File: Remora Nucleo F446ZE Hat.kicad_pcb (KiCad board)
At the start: 2 copper layers, 108.2 x 137.1 mm, 95 parts, among them J1 NucleoF446ZE CN11 Header, J10 A_STEP_AND_DIR+-, J11 B_STEP_AND_DIR+-, J12 C_STEP_AND_DIR+-, J13 DIGITAL_OUTPUTS, J15 Digital Inputs, J16 5V External Power Inlet, J17 9V External Power Inlet, J2 MSD-1-A, J3 UART_TX, J4 NucleoF446ZE CN12 Header, J7 X_STEP_AND_DIR+-, J8 Y_STEP_AND_DIR+-, J9 Z_STEP_AND_DIR+-, SW1 SW_Push, U10 ADUM1201ARZ, U11 HT26LS31ARZ, U12 ADUM1201ARZ, U13 ADUM1201ARZ, U14 HT26LS31ARZ, U19 LTV-247, U20 LTV-247, U21 LTV-247, U22 LTV-247, U4 ADUM1201ARZ, U5 ADUM1201ARZ, U6 HT26LS31ARZ, U7 LTV-247, U8 LTV-247, U9 ADUM1201ARZ

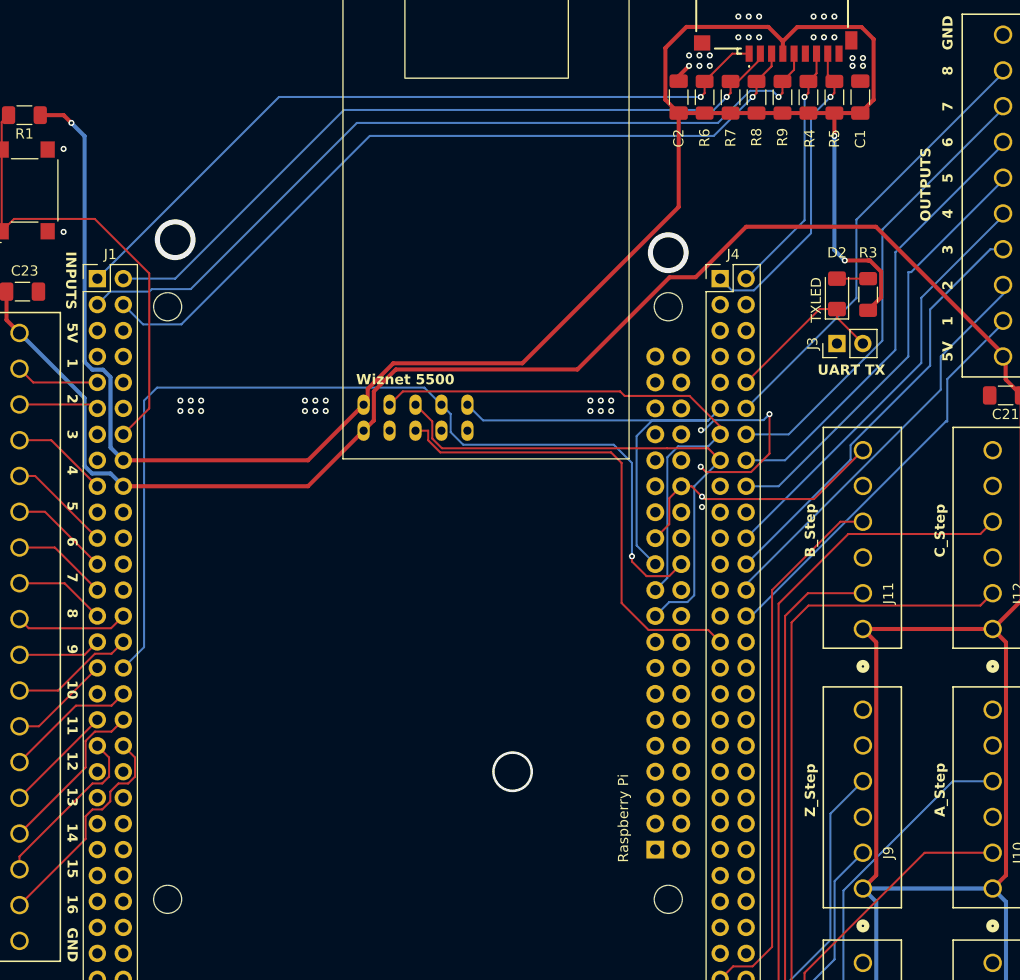
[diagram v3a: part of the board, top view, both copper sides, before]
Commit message: Renumbered IO to start at 0 to match firmware
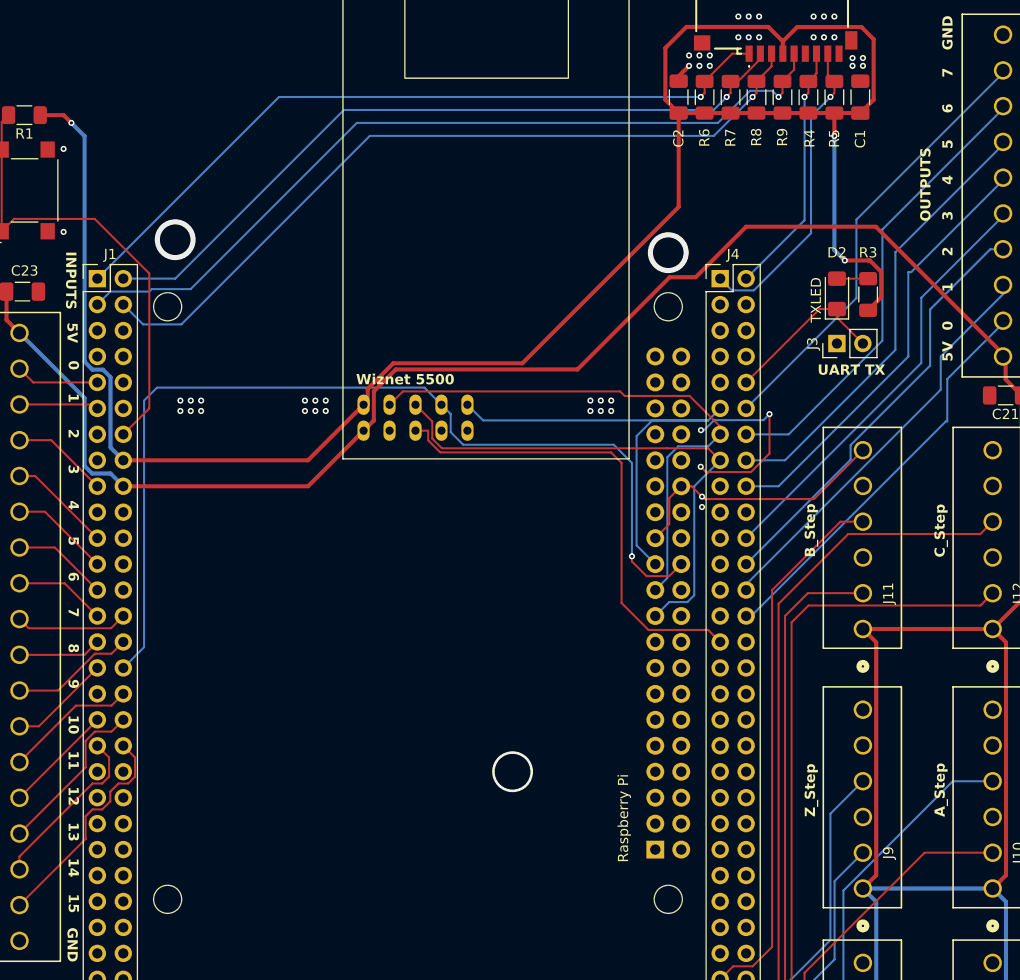
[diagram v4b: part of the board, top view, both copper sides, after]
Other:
- board text added: "0"
- board text removed: "16"
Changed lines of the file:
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@@
 	)
 	(gr_text "1"
-		(at 103.632 73.827 270)
+		(at 103.749339 77.238 270)
 		(layer "F.SilkS")
 		(effects
@@
 	)
 	(gr_text "14"
-		(at 103.632 119.327 270)
+		(at 103.749339 122.738 270)
 		(layer "F.SilkS")
 		(effects
@@
 	)
 	(gr_text "13"
-		(at 103.632 115.827 270)
+		(at 103.749339 119.238 270)
 		(layer "F.SilkS")
 		(effects
@@
 	)
 	(gr_text "1"
-		(at 190.5 70.668 90)
+		(at 190.5 67.355 90)
 		(layer "F.SilkS")
 		(effects
@@
 	)
 	(gr_text "10"
-		(at 103.632 105.327 270)
+		(at 103.749339 108.738 270)
 		(layer "F.SilkS")
 		(effects
@@
 	)
 	(gr_text "7"
-		(at 190.5 49.668 90)
+		(at 190.5 46.355 90)
 		(layer "F.SilkS")
 		(effects
@@
 	)
 	(gr_text "5"
-		(at 103.632 87.827 270)
+		(at 103.749339 91.238 270)
 		(layer "F.SilkS")
 		(effects
@@
 	)
 	(gr_text "15"
-		(at 103.641661 122.827 270)
+		(at 103.759 126.238 270)
 		(layer "F.SilkS")
 		(effects
@@
 	)
 	(gr_text "4"
-		(at 103.632 84.327 270)
+		(at 103.749339 87.738 270)
 		(layer "F.SilkS")
 		(effects
@@
 	)
 	(gr_text "5"
-		(at 190.5 56.668 90)
+		(at 190.5 53.355 90)
 		(layer "F.SilkS")
 		(effects
@@
 	)
 	(gr_text "7"
-		(at 103.632 94.827 270)
+		(at 103.749339 98.238 270)
 		(layer "F.SilkS")
 		(effects
@@
 		)
 	)
-	(gr_text "8"
-		(at 190.5 46.168 90)
+	(gr_text "0"
+		(at 103.759 74.041 270)
 		(layer "F.SilkS")
 		(effects
@@
 	)
 	(gr_text "2"
-		(at 103.632 77.327 270)
+		(at 103.749339 80.738 270)
 		(layer "F.SilkS")
 		(effects
@@
 	)
 	(gr_text "6"
-		(at 103.632 91.327 270)
+		(at 103.749339 94.738 270)
 		(layer "F.SilkS")
 		(effects
@@
 	)
 	(gr_text "8"
-		(at 103.632 98.327 270)
+		(at 103.749339 101.738 270)
 		(layer "F.SilkS")
 		(effects
@@
 	)
 	(gr_text "9"
-		(at 103.632 101.827 270)
+		(at 103.749339 105.238 270)
 		(layer "F.SilkS")
 		(effects
@@
 	)
 	(gr_text "2"
-		(at 190.5 67.168 90)
+		(at 190.5 63.855 90)
 		(layer "F.SilkS")
 		(effects
@@
 	)
 	(gr_text "4"
-		(at 190.5 60.168 90)
+		(at 190.5 56.855 90)
 		(layer "F.SilkS")
 		(effects
@@
 	)
 	(gr_text "3"
-		(at 190.5 63.668 90)
+		(at 190.5 60.355 90)
 		(layer "F.SilkS")
 		(effects
@@
 	)
 	(gr_text "3"
-		(at 103.632 80.827 270)
+		(at 103.749339 84.238 270)
 		(layer "F.SilkS")
 		(effects
@@
 	)
 	(gr_text "11"
-		(at 103.632 108.827 270)
+		(at 103.749339 112.238 270)
 		(layer "F.SilkS")
 		(effects
@@
 	)
 	(gr_text "12"
-		(at 103.632 112.327 270)
+		(at 103.749339 115.738 270)
 		(layer "F.SilkS")
 		(effects
@@
 	)
 	(gr_text "6"
-		(at 190.5 53.168 90)
+		(at 190.5 49.855 90)
 		(layer "F.SilkS")
 		(effects
@@
 		)
 	)
-	(gr_text "16"
-		(at 103.641661 126.327 270)
-		(layer "F.SilkS")
-		(effects
+	(gr_text "0"
+		(at 190.5 71.12 90)
+		(layer "F.SilkS")
+		(effects

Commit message: more BOM consolidation. Switched out IO for vertical toolless wire to board terminals and added footprints. Put new isolated ground plane on board.
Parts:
- J16: value 5V External Power Inlet -> 5V EXT
- J17: value 9V External Power Inlet -> 9V EXT
- moved F1 198.9 mm to (257.3, 33.3)
- moved F2 198.9 mm to (257.3, 35.8)
- moved F3 198.9 mm to (257.3, 38.3)
- moved F4 198.9 mm to (257.3, 40.8)
- moved C13 198.9 mm to (241.9, 48.9)
- moved C14 198.9 mm to (241.9, 52.3)
- moved C15 198.9 mm to (241.9, 55.6)
- moved C16 198.9 mm to (241.9, 59.0)
- moved F5 198.9 mm to (235.5, 33.3)
- moved F6 198.9 mm to (235.5, 35.8)
- moved F7 198.9 mm to (235.5, 38.3)
- moved F8 198.9 mm to (235.5, 40.8)
- moved R16 198.9 mm to (242.6, 33.7)
- moved R17 198.9 mm to (242.6, 37.0)
- moved R18 198.9 mm to (242.6, 40.3)
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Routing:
- net +5VD: track 299.9 -> 0.00 mm
- net +3V3: track 193.5 -> 0.00 mm, vias 3 -> 1
- net /SPI1_CS: track 94.9 -> 0.00 mm, vias 1 -> 0
- net /SDIO_CLK: track 80.5 -> 0.00 mm, vias 1 -> 0
- net /SDIO_CMD: track 76.6 -> 0.00 mm, vias 1 -> 0
- net /SDIO_D2: track 73.6 -> 0.00 mm, vias 1 -> 0
- net /SDIO_D3: track 72.5 -> 0.00 mm, vias 1 -> 0
- net /MCU_C_DIR: track 67.4 -> 0.00 mm
- net /MCU_C_STEP: track 65.8 -> 0.00 mm
- net /MCU_B_STEP: track 57.2 -> 0.00 mm
- net /SPI1_MISO: track 54.7 -> 0.00 mm
- net /MCU_B_DIR: track 53.0 -> 0.00 mm
- net /SPI1_MOSI: track 52.0 -> 0.00 mm
- net /WIZ_RST: track 47.4 -> 0.00 mm
- net GNDREF: track 47.2 -> 0.00 mm, vias 56 -> 9
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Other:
- board size 108.2 x 137.1 mm -> 108 x 162 mm
- board text added: "STATUS"
- board text removed: "USR LED"

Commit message: Swapped out stepper isolators to use same as others. further BOM consolidation. Fixed bug with incorrect differential driver footprint.
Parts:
- removed C10, C16, C17, C18, C20, C9: 100nF, Capacitor_SMD:C_1206_3216Metric_Pad1.33x1.80mm_HandSolder
- removed R1: 10K, Resistor_SMD:R_1206_3216Metric_Pad1.30x1.75mm_HandSolder
- removed R15: 150R, Resistor_SMD:R_1206_3216Metric_Pad1.30x1.75mm_HandSolder
- removed R16, R17, R18, R19, R20, R21, R22, R23: 120R, Resistor_SMD:R_1206_3216Metric_Pad1.30x1.75mm_HandSolder
- removed R2, R3: 100R, Resistor_SMD:R_1206_3216Metric_Pad1.30x1.75mm_HandSolder
- removed U10, U12, U13: ADUM1201ARZ, Package_SO:SOIC-8_3.9x4.9mm_P1.27mm
- added J18: Conn_01x04_Socket, Amphenol QT:QT04ADP83V0000G, F.Cu at (352.0, 76.3)
- added J19: Conn_01x02_Socket, Amphenol QT:QT02ADP83V0000G, F.Cu at (336.9, 9.77)
- added J20: Conn_01x04_Socket, Amphenol QT:QT04ADP83V0000G, F.Cu at (313.8, 9.77)
- added J21: Conn_01x04_Socket, Amphenol QT:QT04ADP83V0000G, F.Cu at (313.8, 25.9)
- added J22: Conn_01x04_Socket, Amphenol QT:QT04ADP83V0000G, F.Cu at (313.8, 42.0)
- added J23: Conn_01x04_Socket, Amphenol QT:QT04ADP83V0000G, F.Cu at (313.8, 58.1)
- added J24: Conn_01x04_Socket, Amphenol QT:QT04ADP83V0000G, F.Cu at (313.8, 76.3)
- added J25: Conn_01x02_Socket, Amphenol QT:QT02ADP83V0000G, F.Cu at (336.9, 76.3)
- added J26: Conn_01x04_Socket, Amphenol QT:QT04ADP83V0000G, F.Cu at (313.8, 92.4)
- added J27: Conn_01x02_Socket, Amphenol QT:QT02ADP83V0000G, F.Cu at (365.1, 92.4)
- added J28: Conn_01x04_Socket, Amphenol QT:QT04ADP83V0000G, F.Cu at (386.7, 25.9)
- added J29: Conn_01x02_Socket, Amphenol QT:QT02ADP83V0000G, F.Cu at (399.8, 42.0)
- added R44: 4K7, Resistor_SMD:R_1206_3216Metric_Pad1.30x1.75mm_HandSolder, F.Cu at (392.5, 89.4)
- added R45: 180R, Resistor_SMD:R_1206_3216Metric_Pad1.30x1.75mm_HandSolder, F.Cu at (392.5, 74.2)
- added R46: 180R, Resistor_SMD:R_1206_3216Metric_Pad1.30x1.75mm_HandSolder, F.Cu at (384.5, 74.2)
- added R47: 180R, Resistor_SMD:R_1206_3216Metric_Pad1.30x1.75mm_HandSolder, F.Cu at (392.5, 77.5)
- added R48: 180R, Resistor_SMD:R_1206_3216Metric_Pad1.30x1.75mm_HandSolder, F.Cu at (384.5, 77.5)
- added R49: 180R, Resistor_SMD:R_1206_3216Metric_Pad1.30x1.75mm_HandSolder, F.Cu at (392.5, 80.8)
- added R50: 180R, Resistor_SMD:R_1206_3216Metric_Pad1.30x1.75mm_HandSolder, F.Cu at (384.5, 80.8)
- added R51: 180R, Resistor_SMD:R_1206_3216Metric_Pad1.30x1.75mm_HandSolder, F.Cu at (392.5, 84.1)
- added R52: 180R, Resistor_SMD:R_1206_3216Metric_Pad1.30x1.75mm_HandSolder, F.Cu at (384.5, 84.1)
- added R53: 180R, Resistor_SMD:R_1206_3216Metric_Pad1.30x1.75mm_HandSolder, F.Cu at (392.5, 92.8)
- added R54: 180R, Resistor_SMD:R_1206_3216Metric_Pad1.30x1.75mm_HandSolder, F.Cu at (392.5, 96.1)
- added R55: 180R, Resistor_SMD:R_1206_3216Metric_Pad1.30x1.75mm_HandSolder, F.Cu at (384.5, 68.9)
- added R56: 180R, Resistor_SMD:R_1206_3216Metric_Pad1.30x1.75mm_HandSolder, F.Cu at (376.1, 34.7)
- added R57: 180R, Resistor_SMD:R_1206_3216Metric_Pad1.30x1.75mm_HandSolder, F.Cu at (376.1, 85.0)
- added R58: 180R, Resistor_SMD:R_1206_3216Metric_Pad1.30x1.75mm_HandSolder, F.Cu at (410.8, 34.7)
- added R59: 180R, Resistor_SMD:R_1206_3216Metric_Pad1.30x1.75mm_HandSolder, F.Cu at (376.1, 38.0)
- added R60: 180R, Resistor_SMD:R_1206_3216Metric_Pad1.30x1.75mm_HandSolder, F.Cu at (376.1, 88.3)
- added R61: 180R, Resistor_SMD:R_1206_3216Metric_Pad1.30x1.75mm_HandSolder, F.Cu at (410.8, 38.0)
- added R62: 180R, Resistor_SMD:R_1206_3216Metric_Pad1.30x1.75mm_HandSolder, F.Cu at (376.1, 41.3)
- added R63: 180R, Resistor_SMD:R_1206_3216Metric_Pad1.30x1.75mm_HandSolder, F.Cu at (376.1, 91.6)
- added R64: 180R, Resistor_SMD:R_1206_3216Metric_Pad1.30x1.75mm_HandSolder, F.Cu at (410.8, 41.3)
- added R65: 180R, Resistor_SMD:R_1206_3216Metric_Pad1.30x1.75mm_HandSolder, F.Cu at (376.1, 44.6)
- added R66: 180R, Resistor_SMD:R_1206_3216Metric_Pad1.30x1.75mm_HandSolder, F.Cu at (376.1, 94.9)
- added R67: 180R, Resistor_SMD:R_1206_3216Metric_Pad1.30x1.75mm_HandSolder, F.Cu at (410.8, 44.6)
- D1: value USR_LED -> LED
- D2: value TXLED -> LED
- D5: value 9VLED -> LED
- D6: value 5VLED -> LED
- J1: value NucleoF446ZE CN11 Header -> Conn_02x35_Odd_Even
- J10: value A_STEP_AND_DIR+- -> Conn_01x02_Socket; footprint EBWA_06_A:CONN_EBWA-06-A_ADM -> Amphenol QT:QT02ADP83V0000G
- J11: value B_STEP_AND_DIR+- -> Conn_01x04_Socket; footprint EBWA_06_A:CONN_EBWA-06-A_ADM -> Amphenol QT:QT04ADP83V0000G
- J12: value C_STEP_AND_DIR+- -> Conn_01x02_Socket; footprint EBWA_06_A:CONN_EBWA-06-A_ADM -> Amphenol QT:QT02ADP83V0000G
- J13: value DIGITAL_OUTPUTS -> Conn_01x02_Socket; footprint EBWA_06_A:CONN_EBWA-10-A_ADM -> Amphenol QT:QT02ADP83V0000G
- J15: value Digital Inputs -> Conn_01x02_Socket; footprint EBWA_06_A:CONN_EBWA-18-A_ADM -> Amphenol QT:QT02ADP83V0000G
- J16: value 5V EXT -> Conn_01x04_Socket; footprint EBWA_02_A:ADAMTECH_EBWA-02-A -> Amphenol QT:QT04ADP83V0000G
- J17: value 9V EXT -> Conn_01x02_Socket; footprint EBWA_02_A:ADAMTECH_EBWA-02-A -> Amphenol QT:QT02ADP83V0000G
- J4: value NucleoF446ZE CN12 Header -> Conn_02x35_Odd_Even
- J7: value X_STEP_AND_DIR+- -> Conn_01x04_Socket; footprint EBWA_06_A:CONN_EBWA-06-A_ADM -> Amphenol QT:QT04ADP83V0000G
- J8: value Y_STEP_AND_DIR+- -> Conn_01x02_Socket; footprint EBWA_06_A:CONN_EBWA-06-A_ADM -> Amphenol QT:QT02ADP83V0000G
- J9: value Z_STEP_AND_DIR+- -> Conn_01x04_Socket; footprint EBWA_06_A:CONN_EBWA-06-A_ADM -> Amphenol QT:QT04ADP83V0000G
- RP1: value Raspberry_Pi_2_3 -> Raspberry_Pi_Header
- U1: value ~ -> Wiznet W5500 Eval Module
- U11, U14, U6: value HT26LS31ARZ -> AM26LS31CDR; footprint Package_DIP:SMDIP-4_W9.53mm -> Package_SO:SOIC-16_3.9x9.9mm_P1.27mm
- U4, U5, U9: value ADUM1201ARZ -> LTV-247; footprint Package_SO:SOIC-8_3.9x4.9mm_P1.27mm -> Package_SO:SOP-16_4.4x10.4mm_P1.27mm
- moved J15 236.1 mm to (399.8, 60.1), turned to 0 degrees
- moved J17 235.1 mm to (365.1, 42.0)
- moved J16 234.4 mm to (352.0, 25.9)
- moved J13 222.1 mm to (386.7, 60.1), turned to 0 degrees
- moved J11 219.0 mm to (386.7, 9.77), turned to 0 degrees
- moved J7 217.2 mm to (352.0, 9.77), turned to 0 degrees
- moved U9 207.5 mm to (409.4, 6.74)
- moved J12 195.4 mm to (386.7, 42.0), turned to 0 degrees
- moved J8 187.1 mm to (352.0, 42.0), turned to 0 degrees
- moved J9 177.3 mm to (352.0, 60.1), turned to 0 degrees
- moved C14 170.1 mm to (407.7, 14.4)
- moved U4 160.0 mm to (374.8, 6.74)
- moved C12 158.6 mm to (373.0, 14.4)
- moved J10 155.3 mm to (352.0, 92.4), turned to 0 degrees
- moved U5 134.9 mm to (374.8, 57.1)
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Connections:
- C13 pad 1: GNDREF -> +5VD
- C13 pad 2: +3V3 -> GNDPWR
- C14 pad 1: GNDREF -> +5VD
- C14 pad 2: +3V3 -> GNDPWR
- F1 pad 2: /Digital Outputs/4CH digital output driver 1/OUTPUT1 -> /Digital Outputs/4CH digital output driver 1/OUTPUT0
- F2 pad 2: /Digital Outputs/4CH digital output driver 1/OUTPUT2 -> /Digital Outputs/4CH digital output driver 1/OUTPUT1
- F3 pad 2: /Digital Outputs/4CH digital output driver 1/OUTPUT3 -> /Digital Outputs/4CH digital output driver 1/OUTPUT2
- F4 pad 2: /Digital Outputs/4CH digital output driver 1/OUTPUT4 -> /Digital Outputs/4CH digital output driver 1/OUTPUT3
- F5 pad 2: /Digital Outputs/4CH digital output driver 2/OUTPUT5 -> /Digital Outputs/4CH digital output driver 2/OUTPUT4
- F6 pad 2: /Digital Outputs/4CH digital output driver 2/OUTPUT6 -> /Digital Outputs/4CH digital output driver 2/OUTPUT5
- F7 pad 2: /Digital Outputs/4CH digital output driver 2/OUTPUT7 -> /Digital Outputs/4CH digital output driver 2/OUTPUT6
- F8 pad 2: /Digital Outputs/4CH digital output driver 2/OUTPUT8 -> /Digital Outputs/4CH digital output driver 2/OUTPUT7
- J1 pad 11: MCU_DIGITAL_IN_2 -> MCU_DIGITAL_IN_1
- J1 pad 17: MCU_DIGITAL_IN_3 -> MCU_DIGITAL_IN_2
- J1 pad 21: MCU_DIGITAL_IN_4 -> MCU_DIGITAL_IN_3
- J1 pad 23: MCU_DIGITAL_IN_5 -> MCU_DIGITAL_IN_4
- J1 pad 25: MCU_DIGITAL_IN_6 -> unconnected-(J1-Pin_25-Pad25)
- J1 pad 27: MCU_DIGITAL_IN_7 -> unconnected-(J1-Pin_27-Pad27)
- J1 pad 28: MCU_DIGITAL_IN_8 -> MCU_DIGITAL_IN_5
- J1 pad 29: MCU_DIGITAL_IN_9 -> unconnected-(J1-Pin_29-Pad29)
- J1 pad 30: MCU_DIGITAL_IN_10 -> MCU_DIGITAL_IN_6
- J1 pad 31: MCU_DIGITAL_IN_11 -> unconnected-(J1-Pin_31-Pad31)
- J1 pad 34: MCU_DIGITAL_IN_12 -> MCU_DIGITAL_IN_7
- J1 pad 35: MCU_DIGITAL_IN_13 -> MCU_DIGITAL_IN_8
- J1 pad 36: MCU_DIGITAL_IN_14 -> MCU_DIGITAL_IN_9
- J1 pad 37: MCU_DIGITAL_IN_15 -> MCU_DIGITAL_IN_10
- J1 pad 38: MCU_DIGITAL_IN_16 -> MCU_DIGITAL_IN_11
- J1 pad 39: unconnected-(J1-Pin_39-Pad39) -> MCU_DIGITAL_IN_12
- J1 pad 40: unconnected-(J1-Pin_40-Pad40) -> MCU_DIGITAL_IN_13
- J1 pad 41: unconnected-(J1-Pin_41-Pad41) -> MCU_DIGITAL_IN_14
- J1 pad 42: unconnected-(J1-Pin_42-Pad42) -> MCU_DIGITAL_IN_15
- J1 pad 9: MCU_DIGITAL_IN_1 -> MCU_DIGITAL_IN_0
- J10 pad 1: +5VD -> /Z and A Stepper Drivers/A_DIR-
- J10 pad 2: /Z and A Stepper Drivers/A_STEP+ -> GNDPWR
- J11 pad 2: /B and C Stepper Drivers/B_STEP+ -> /B and C Stepper Drivers/C_STEP+
- J11 pad 3: /B and C Stepper Drivers/B_STEP- -> /B and C Stepper Drivers/C_STEP-
- J11 pad 4: /B and C Stepper Drivers/B_DIR+ -> /B and C Stepper Drivers/C_DIR+
- J12 pad 1: +5VD -> /B and C Stepper Drivers/C_DIR-
- J12 pad 2: /B and C Stepper Drivers/C_STEP+ -> GNDPWR
- J13 pad 1: +5VD -> GNDPWR
- J13 pad 2: /Digital Outputs/4CH digital output driver 1/OUTPUT1 -> +5VD
- J15 pad 1: +5VD -> GNDREF
- J15 pad 2: /Digital Inputs/Digital Input 1-4/INPUT1 -> +9V
- J16 pad 1: GNDPWR -> +5VD
- J16 pad 2: +5VD -> /X and Y Stepper Drivers/X_STEP+
- J17 pad 1: GNDREF -> /X and Y Stepper Drivers/X_DIR-
- J17 pad 2: +9V -> GNDPWR
- J4 pad 12: MCU_DIGITAL_OUT_8 -> unconnected-(J4-Pin_12-Pad12)
- J4 pad 16: MCU_DIGITAL_OUT_6 -> unconnected-(J4-Pin_16-Pad16)
- J4 pad 17: unconnected-(J4-Pin_17-Pad17) -> MCU_DIGITAL_OUT_6
- J4 pad 18: MCU_DIGITAL_OUT_5 -> unconnected-(J4-Pin_18-Pad18)
- J4 pad 21: unconnected-(J4-Pin_21-Pad21) -> MCU_DIGITAL_OUT_5
- J4 pad 22: MCU_DIGITAL_OUT_4 -> unconnected-(J4-Pin_22-Pad22)
- J4 pad 23: unconnected-(J4-Pin_23-Pad23) -> MCU_DIGITAL_OUT_4
- J4 pad 30: unconnected-(J4-Pin_30-Pad30) -> MCU_DIGITAL_OUT_0
- J4 pad 55: /MCU_B_DIR -> unconnected-(J4-Pin_55-Pad55)
- J4 pad 56: unconnected-(J4-Pin_56-Pad56) -> /MCU_C_DIR
- J4 pad 57: /MCU_B_STEP -> unconnected-(J4-Pin_57-Pad57)
- J4 pad 58: unconnected-(J4-Pin_58-Pad58) -> /MCU_C_STEP
- J4 pad 60: /MCU_C_DIR -> /MCU_B_DIR
- J4 pad 62: /MCU_C_STEP -> /MCU_B_STEP
- J4 pad 65: /USR_LED -> /STATUS_LED
- J7 pad 2: /X and Y Stepper Drivers/X_STEP+ -> /X and Y Stepper Drivers/Y_STEP+
- J7 pad 3: /X and Y Stepper Drivers/X_STEP- -> /X and Y Stepper Drivers/Y_STEP-
- J7 pad 4: /X and Y Stepper Drivers/X_DIR+ -> /X and Y Stepper Drivers/Y_DIR+
- J8 pad 1: +5VD -> /X and Y Stepper Drivers/Y_DIR-
- J8 pad 2: /X and Y Stepper Drivers/Y_STEP+ -> GNDPWR
- J9 pad 2: /Z and A Stepper Drivers/Z_STEP+ -> /Z and A Stepper Drivers/A_STEP+
- J9 pad 3: /Z and A Stepper Drivers/Z_STEP- -> /Z and A Stepper Drivers/A_STEP-
- J9 pad 4: /Z and A Stepper Drivers/Z_DIR+ -> /Z and A Stepper Drivers/A_DIR+
- R28 pad 1: /Digital Inputs/Digital Input 1-4/INPUT1 -> /Digital Inputs/Digital Input 0-3/INPUT0
- R29 pad 1: /Digital Inputs/Digital Input 1-4/INPUT2 -> /Digital Inputs/Digital Input 0-3/INPUT1
- R30 pad 1: /Digital Inputs/Digital Input 1-4/INPUT3 -> /Digital Inputs/Digital Input 0-3/INPUT2
- R31 pad 1: /Digital Inputs/Digital Input 1-4/INPUT4 -> /Digital Inputs/Digital Input 0-3/INPUT3
- R32 pad 1: /Digital Inputs/Digital Input 5-8/INPUT5 -> /Digital Inputs/Digital Input 4-7/INPUT4
- R33 pad 1: /Digital Inputs/Digital Input 5-8/INPUT6 -> /Digital Inputs/Digital Input 4-7/INPUT5
- R34 pad 1: /Digital Inputs/Digital Input 5-8/INPUT7 -> /Digital Inputs/Digital Input 4-7/INPUT6
- R35 pad 1: /Digital Inputs/Digital Input 5-8/INPUT8 -> /Digital Inputs/Digital Input 4-7/INPUT7
- R36 pad 1: /Digital Inputs/Digital Input 9-12/INPUT9 -> /Digital Inputs/Digital Input 8-11/INPUT8
- R37 pad 1: /Digital Inputs/Digital Input 9-12/INPUT10 -> /Digital Inputs/Digital Input 8-11/INPUT9
- R38 pad 1: /Digital Inputs/Digital Input 9-12/INPUT11 -> /Digital Inputs/Digital Input 8-11/INPUT10
- R39 pad 1: /Digital Inputs/Digital Input 9-12/INPUT12 -> /Digital Inputs/Digital Input 8-11/INPUT11
- R40 pad 1: /Digital Inputs/Digital Input 13-16/INPUT13 -> /Digital Inputs/Digital Input 12-15/INPUT12
- R41 pad 1: /Digital Inputs/Digital Input 13-16/INPUT14 -> /Digital Inputs/Digital Input 12-15/INPUT13
- R42 pad 1: /Digital Inputs/Digital Input 13-16/INPUT15 -> /Digital Inputs/Digital Input 12-15/INPUT14
- R43 pad 1: /Digital Inputs/Digital Input 13-16/INPUT16 -> /Digital Inputs/Digital Input 12-15/INPUT15
- U14 pad 1: Net-(U12-VOA) -> Net-(U14-1A)
- U19 pad 10: MCU_DIGITAL_IN_8 -> MCU_DIGITAL_IN_7
- U19 pad 12: MCU_DIGITAL_IN_7 -> MCU_DIGITAL_IN_6
- U19 pad 14: MCU_DIGITAL_IN_6 -> MCU_DIGITAL_IN_5
- U19 pad 16: MCU_DIGITAL_IN_5 -> MCU_DIGITAL_IN_4
- U20 pad 10: MCU_DIGITAL_IN_12 -> MCU_DIGITAL_IN_11
- U20 pad 12: MCU_DIGITAL_IN_11 -> MCU_DIGITAL_IN_10
- U20 pad 14: MCU_DIGITAL_IN_10 -> MCU_DIGITAL_IN_9
- U20 pad 16: MCU_DIGITAL_IN_9 -> MCU_DIGITAL_IN_8
- U21 pad 10: MCU_DIGITAL_IN_16 -> MCU_DIGITAL_IN_15
- U21 pad 12: MCU_DIGITAL_IN_15 -> MCU_DIGITAL_IN_14
- U21 pad 14: MCU_DIGITAL_IN_14 -> MCU_DIGITAL_IN_13
- U21 pad 16: MCU_DIGITAL_IN_13 -> MCU_DIGITAL_IN_12
- U22 pad 10: MCU_DIGITAL_IN_4 -> MCU_DIGITAL_IN_3
- U22 pad 12: MCU_DIGITAL_IN_3 -> MCU_DIGITAL_IN_2
- U22 pad 14: MCU_DIGITAL_IN_2 -> MCU_DIGITAL_IN_1
- U22 pad 16: MCU_DIGITAL_IN_1 -> MCU_DIGITAL_IN_0
- U4 pad 1: +3V3 -> Net-(R56-Pad2)
- U4 pad 2: /MCU_X_STEP -> GNDREF
- U4 pad 3: /MCU_X_DIR -> Net-(R59-Pad2)
- U4 pad 5: GNDPWR -> Net-(R62-Pad2)
- U4 pad 6: Net-(U4-VOB) -> GNDREF
- U4 pad 7: Net-(U4-VOA) -> Net-(R65-Pad2)
- U4 pad 8: +5VD -> GNDREF
- U5 pad 1: +3V3 -> Net-(R57-Pad2)
- U5 pad 2: /MCU_Y_STEP -> GNDREF
- U5 pad 3: /MCU_Y_DIR -> Net-(R60-Pad2)
- U5 pad 5: GNDPWR -> Net-(R63-Pad2)
- U5 pad 6: Net-(U5-VOB) -> GNDREF
- U5 pad 8: +5VD -> GNDREF
- U6 pad 1: Net-(U4-VOA) -> Net-(U6-1A)
- U9 pad 1: +3V3 -> Net-(R58-Pad2)
- U9 pad 2: /MCU_Z_STEP -> GNDREF
- U9 pad 3: /MCU_Z_DIR -> Net-(R61-Pad2)
- U9 pad 5: GNDPWR -> Net-(R64-Pad2)
- U9 pad 6: Net-(U11-2A) -> GNDREF
- U9 pad 7: Net-(U11-1A) -> Net-(R67-Pad2)
- U9 pad 8: +5VD -> GNDREF
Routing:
- net unconnected-(J4-Pin_23-Pad23): vias 1 -> 0
- net MCU_DIGITAL_OUT_4: vias 0 -> 1

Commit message: New PSU schematics
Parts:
- added C16: 100nF, Capacitor_SMD:C_1206_3216Metric_Pad1.33x1.80mm_HandSolder, F.Cu at (202.8, -49.6)
- added C17: 100nF, Capacitor_SMD:C_1206_3216Metric_Pad1.33x1.80mm_HandSolder, F.Cu at (202.8, -18.8)
- added C18: 100nF, Capacitor_SMD:C_1206_3216Metric_Pad1.33x1.80mm_HandSolder, F.Cu at (202.8, -34.2)
- added C20: 100nF, Capacitor_SMD:C_1206_3216Metric_Pad1.33x1.80mm_HandSolder, F.Cu at (202.8, -46.2)
- added C24: 100nF, Capacitor_SMD:C_1206_3216Metric_Pad1.33x1.80mm_HandSolder, F.Cu at (202.8, -15.4)
- added C25: 100nF, Capacitor_SMD:C_1206_3216Metric_Pad1.33x1.80mm_HandSolder, F.Cu at (202.8, -30.9)
- added C32: 100nF, Capacitor_SMD:C_1206_3216Metric_Pad1.33x1.80mm_HandSolder, F.Cu at (202.8, -42.9)
- added C33: 100nF, Capacitor_SMD:C_1206_3216Metric_Pad1.33x1.80mm_HandSolder, F.Cu at (202.8, -12.1)
- added C34: 100nF, Capacitor_SMD:C_1206_3216Metric_Pad1.33x1.80mm_HandSolder, F.Cu at (202.8, -27.5)
- added C38: 100nF, Capacitor_SMD:C_1206_3216Metric_Pad1.33x1.80mm_HandSolder, F.Cu at (202.8, -39.5)
- added C39: 100nF, Capacitor_SMD:C_1206_3216Metric_Pad1.33x1.80mm_HandSolder, F.Cu at (202.8, -8.75)
- added C40: 100nF, Capacitor_SMD:C_1206_3216Metric_Pad1.33x1.80mm_HandSolder, F.Cu at (202.8, -24.1)
- added R100: 4K7, Resistor_SMD:R_1206_3216Metric_Pad1.30x1.75mm_HandSolder, F.Cu at (214.8, -27.6)
- added R101: 4K7, Resistor_SMD:R_1206_3216Metric_Pad1.30x1.75mm_HandSolder, F.Cu at (214.8, -39.7)
- added R102: 4K7, Resistor_SMD:R_1206_3216Metric_Pad1.30x1.75mm_HandSolder, F.Cu at (214.8, -8.89)
- added R103: 4K7, Resistor_SMD:R_1206_3216Metric_Pad1.30x1.75mm_HandSolder, F.Cu at (214.8, -24.3)
- added R104: 4K7, Resistor_SMD:R_1206_3216Metric_Pad1.30x1.75mm_HandSolder, F.Cu at (220.7, -49.6)
- added R105: 4K7, Resistor_SMD:R_1206_3216Metric_Pad1.30x1.75mm_HandSolder, F.Cu at (220.7, -46.3)
- added R106: 4K7, Resistor_SMD:R_1206_3216Metric_Pad1.30x1.75mm_HandSolder, F.Cu at (220.7, -43.0)
- added R107: 4K7, Resistor_SMD:R_1206_3216Metric_Pad1.30x1.75mm_HandSolder, F.Cu at (220.7, -39.7)
- added R108: 4K7, Resistor_SMD:R_1206_3216Metric_Pad1.30x1.75mm_HandSolder, F.Cu at (220.7, -18.8)
- added R109: 4K7, Resistor_SMD:R_1206_3216Metric_Pad1.30x1.75mm_HandSolder, F.Cu at (220.7, -15.5)
- added R110: 4K7, Resistor_SMD:R_1206_3216Metric_Pad1.30x1.75mm_HandSolder, F.Cu at (220.7, -12.2)
- added R111: 4K7, Resistor_SMD:R_1206_3216Metric_Pad1.30x1.75mm_HandSolder, F.Cu at (220.7, -8.89)
- added R112: 4K7, Resistor_SMD:R_1206_3216Metric_Pad1.30x1.75mm_HandSolder, F.Cu at (220.7, -34.2)
- added R113: 4K7, Resistor_SMD:R_1206_3216Metric_Pad1.30x1.75mm_HandSolder, F.Cu at (220.7, -30.9)
- added R114: 4K7, Resistor_SMD:R_1206_3216Metric_Pad1.30x1.75mm_HandSolder, F.Cu at (220.7, -27.6)
- added R115: 4K7, Resistor_SMD:R_1206_3216Metric_Pad1.30x1.75mm_HandSolder, F.Cu at (220.7, -24.3)
- added R80: 180R, Resistor_SMD:R_1206_3216Metric_Pad1.30x1.75mm_HandSolder, F.Cu at (208.8, -49.6)
- added R81: 180R, Resistor_SMD:R_1206_3216Metric_Pad1.30x1.75mm_HandSolder, F.Cu at (208.8, -18.8)
- added R82: 180R, Resistor_SMD:R_1206_3216Metric_Pad1.30x1.75mm_HandSolder, F.Cu at (208.8, -34.2)
- added R83: 180R, Resistor_SMD:R_1206_3216Metric_Pad1.30x1.75mm_HandSolder, F.Cu at (208.8, -46.3)
- added R84: 180R, Resistor_SMD:R_1206_3216Metric_Pad1.30x1.75mm_HandSolder, F.Cu at (208.8, -15.5)
- added R85: 180R, Resistor_SMD:R_1206_3216Metric_Pad1.30x1.75mm_HandSolder, F.Cu at (208.8, -30.9)
- added R86: 180R, Resistor_SMD:R_1206_3216Metric_Pad1.30x1.75mm_HandSolder, F.Cu at (208.8, -43.0)
- added R87: 180R, Resistor_SMD:R_1206_3216Metric_Pad1.30x1.75mm_HandSolder, F.Cu at (208.8, -12.2)
- added R88: 180R, Resistor_SMD:R_1206_3216Metric_Pad1.30x1.75mm_HandSolder, F.Cu at (208.8, -27.6)
- added R89: 180R, Resistor_SMD:R_1206_3216Metric_Pad1.30x1.75mm_HandSolder, F.Cu at (208.8, -39.7)
- added R90: 180R, Resistor_SMD:R_1206_3216Metric_Pad1.30x1.75mm_HandSolder, F.Cu at (208.8, -8.89)
- added R91: 180R, Resistor_SMD:R_1206_3216Metric_Pad1.30x1.75mm_HandSolder, F.Cu at (208.8, -24.3)
- added R92: 4K7, Resistor_SMD:R_1206_3216Metric_Pad1.30x1.75mm_HandSolder, F.Cu at (214.8, -49.6)
- added R93: 4K7, Resistor_SMD:R_1206_3216Metric_Pad1.30x1.75mm_HandSolder, F.Cu at (214.8, -18.8)
- added R94: 4K7, Resistor_SMD:R_1206_3216Metric_Pad1.30x1.75mm_HandSolder, F.Cu at (214.8, -34.2)
- added R95: 4K7, Resistor_SMD:R_1206_3216Metric_Pad1.30x1.75mm_HandSolder, F.Cu at (214.8, -46.3)
- added R96: 4K7, Resistor_SMD:R_1206_3216Metric_Pad1.30x1.75mm_HandSolder, F.Cu at (214.8, -15.5)
- added R97: 4K7, Resistor_SMD:R_1206_3216Metric_Pad1.30x1.75mm_HandSolder, F.Cu at (214.8, -30.9)
- added R98: 4K7, Resistor_SMD:R_1206_3216Metric_Pad1.30x1.75mm_HandSolder, F.Cu at (214.8, -43.0)
- added R99: 4K7, Resistor_SMD:R_1206_3216Metric_Pad1.30x1.75mm_HandSolder, F.Cu at (214.8, -12.2)

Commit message: New PSU designs + footprints assigned. Changes to board shape to make room for new components. BOM consolidation of supplimentary file
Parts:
- removed the J13 at (386.7, 60.1)
- removed the J15 at (399.8, 60.1)
- added C3: 470uF, Capacitor_THT:CP_Radial_D8.0mm_P3.50mm, F.Cu at (470.1, 143.9)
- added C4: 470uF, Capacitor_THT:CP_Radial_D8.0mm_P3.50mm, F.Cu at (470.1, 153.4)
- added C5: 1uF, Capacitor_SMD:C_1206_3216Metric_Pad1.33x1.80mm_HandSolder, F.Cu at (460.1, 169.2)
- added C6: 1uF, Capacitor_SMD:C_1206_3216Metric_Pad1.33x1.80mm_HandSolder, F.Cu at (460.1, 172.5)
- added C7: 180uF, Capacitor_THT:CP_Radial_D6.3mm_P2.50mm, F.Cu at (487.5, 162.2)
- added C8: 180uF, Capacitor_THT:CP_Radial_D6.3mm_P2.50mm, F.Cu at (487.5, 170.0)
- added D3: B330AF, Diode_SMD:D_SMA, F.Cu at (461.2, 160.7)
- added D4: B330AF, Diode_SMD:D_SMA, F.Cu at (461.2, 165.2)
- added J5: 24V Logic, EBWA_02_A:ADAMTECH_EBWA-02-A, F.Cu at (471.2, 162.8)
- added J6: 24V Peripheral, EBWA_02_A:ADAMTECH_EBWA-02-A, F.Cu at (480.1, 162.8)
- added JP1: Peripheral->Logic VDD Jumper, Jumper:SolderJumper-2_P1.3mm_Bridged2Bar_RoundedPad1.0x1.5mm, F.Cu at (478.8, 140.9)
- added JP2: Peripheral->Logic VDD Jumper, Jumper:SolderJumper-2_P1.3mm_Bridged2Bar_RoundedPad1.0x1.5mm, F.Cu at (478.8, 144.4)
- added JP3: Peripheral->Logic VDD Jumper, Jumper:SolderJumper-2_P1.3mm_Open_RoundedPad1.0x1.5mm, F.Cu at (478.8, 148.0)
- added JP4: Peripheral->Logic GND Jumper, Jumper:SolderJumper-2_P1.3mm_Open_RoundedPad1.0x1.5mm, F.Cu at (478.8, 151.6)
- added L1: 68uH / 1A, Inductor_SMD:L_APV_ANR8040, F.Cu at (462.0, 143.9)
- added L2: 68uH / 1A, Inductor_SMD:L_APV_ANR8040, F.Cu at (462.0, 153.6)
- added U2: XL1509-12, Package_SO:SOIC-8_3.9x4.9mm_P1.27mm, F.Cu at (485.2, 142.5)
- added U3: XL1509-5.0, Package_SO:SOIC-8_3.9x4.9mm_P1.27mm, F.Cu at (485.2, 149.1)
- moved C27 414.1 mm to (575.8, 122.7)
- moved C15 391.8 mm to (628.2, 120.8)
- moved C21 391.8 mm to (607.1, 142.6)
- moved C29 391.8 mm to (552.4, 215.0)
- moved C9 391.8 mm to (607.1, 120.8)
- moved D5 391.8 mm to (628.2, 144.9)
- moved D6 391.8 mm to (628.2, 148.3)
- moved R20 391.8 mm to (601.1, 15.6)
- moved R22 391.8 mm to (601.1, 18.9)
- moved R24 391.8 mm to (601.1, 22.2)
- moved R26 391.8 mm to (601.1, 25.5)
- moved R44 391.8 mm to (648.0, 151.1)
- moved R45 391.8 mm to (648.0, 154.4)
- moved R46 391.8 mm to (648.0, 157.8)
- moved R47 391.8 mm to (648.0, 161.1)
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- renumbered C12 to C10, C16 to C11, C32 to C12, C20 to C13, C38 to C14, C13 to C16, C33 to C18, C24 to C19, C39 to C20, C19 to C21, C14 to C22, C18 to C23, C34 to C24, C40 to C26, C21 to C27, C23 to C29, C11 to C9, J8 to J10, J18 to J11, J27 to J12, J9 to J13, J10 to J14, J28 to J15, J29 to J16, J11 to J17, J12 to J18, J24 to J19, J26 to J20, J25 to J21, J20 to J23, J21 to J24, J22 to J25, J23 to J26, J19 to J27, J16 to J7, J17 to J8, J7 to J9, R44 to R1, R14 to R10, R55 to R11, R56 to R12, R59 to R13, R62 to R14, R65 to R15, R80 to R16, R83 to R17, R86 to R18, R89 to R19, R53 to R2, R92 to R20, R104 to R21, R95 to R22, R105 to R23, R98 to R24, R106 to R25, R101 to R26, R107 to R27, R45 to R28, R47 to R29, R54 to R3, R49 to R30, R51 to R31, R46 to R36, R48 to R37, R50 to R38, R52 to R39, R36 to R40, R37 to R41, R38 to R42, R39 to R43, R40 to R44, R41 to R45, R42 to R46, R43 to R47, R57 to R48, R60 to R49, R63 to R50, R66 to R51, R81 to R52, R84 to R53, R87 to R54, R90 to R55, R93 to R56, R108 to R57, R96 to R58, R109 to R59, R99 to R60, R110 to R61, R102 to R62, R111 to R63, R58 to R64, R61 to R65, R64 to R66, R82 to R68, R85 to R69, R88 to R70, R91 to R71, R94 to R72, R112 to R73, R97 to R74, R113 to R75, R100 to R76, R114 to R77, R103 to R78, R115 to R79, R28 to R84, R29 to R85, R30 to R86, R31 to R87, U21 to U10, U5 to U11, U11 to U12, U9 to U13, U22 to U19, U6 to U5, U7 to U6, U19 to U7, U20 to U9
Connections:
- J1 pad 24: unconnected-(J1-Pin_24-Pad24) -> +12V
- R10 pad 1: +9V -> +12V
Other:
- board size 108 x 162 mm -> 138 x 162 mm
